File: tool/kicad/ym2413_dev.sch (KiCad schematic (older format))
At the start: 34 parts, among them P1 CONN_4, U1 YM2413, X1 CRYSTAL

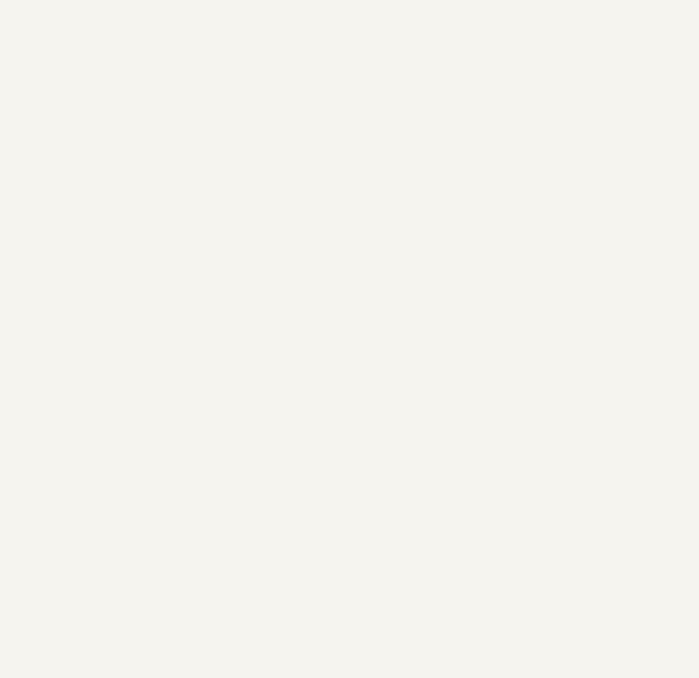
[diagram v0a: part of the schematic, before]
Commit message: add EFM32 to sch
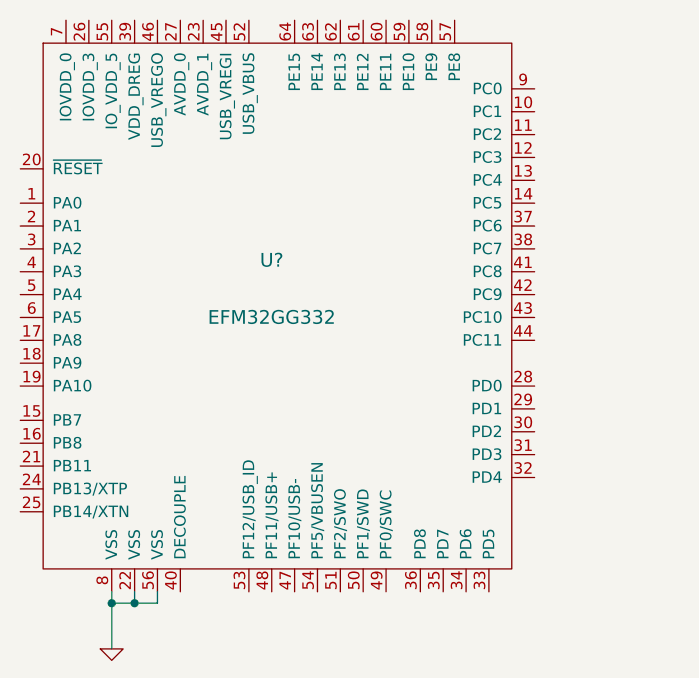
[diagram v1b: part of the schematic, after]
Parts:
- added U?: EFM32GG332, symbol EFM32GG332
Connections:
- wire segments 79 -> 83
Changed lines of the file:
@@
 	1    0    0    -1
 $EndComp
+$Comp
+L EFM32GG332 U?
+U 1 1 52F41304
+P 2500 4050
+F 0 "U?" H 2500 4150 60  0000 C CNN
+F 1 "EFM32GG332" H 2500 3900 60  0000 C CNN
+F 2 "" H 2100 4500 60  0000 C CNN
+F 3 "" H 2100 4500 60  0000 C CNN
+	1    2500 4050
+	1    0    0    -1
+$EndComp
+$Comp
+L GND #PWR?
+U 1 1 52F41311
+P 1800 5650
+F 0 "#PWR?" H 1800 5650 30  0001 C CNN
+F 1 "GND" H 1800 5580 30  0001 C CNN
+F 2 "" H 1800 5650 60  0000 C CNN
+F 3 "" H 1800 5650 60  0000 C CNN
+	1    1800 5650
+	1    0    0    -1
+$EndComp
+Wire Wire Line
+	1800 5650 1800 5400
+Wire Wire Line
+	1800 5450 2000 5450
+Wire Wire Line
+	2000 5450 2000 5400
+Connection ~ 1800 5450
+Wire Wire Line
+	1900 5400 1900 5450
+Connection ~ 1900 5450
 $EndSCHEMATC

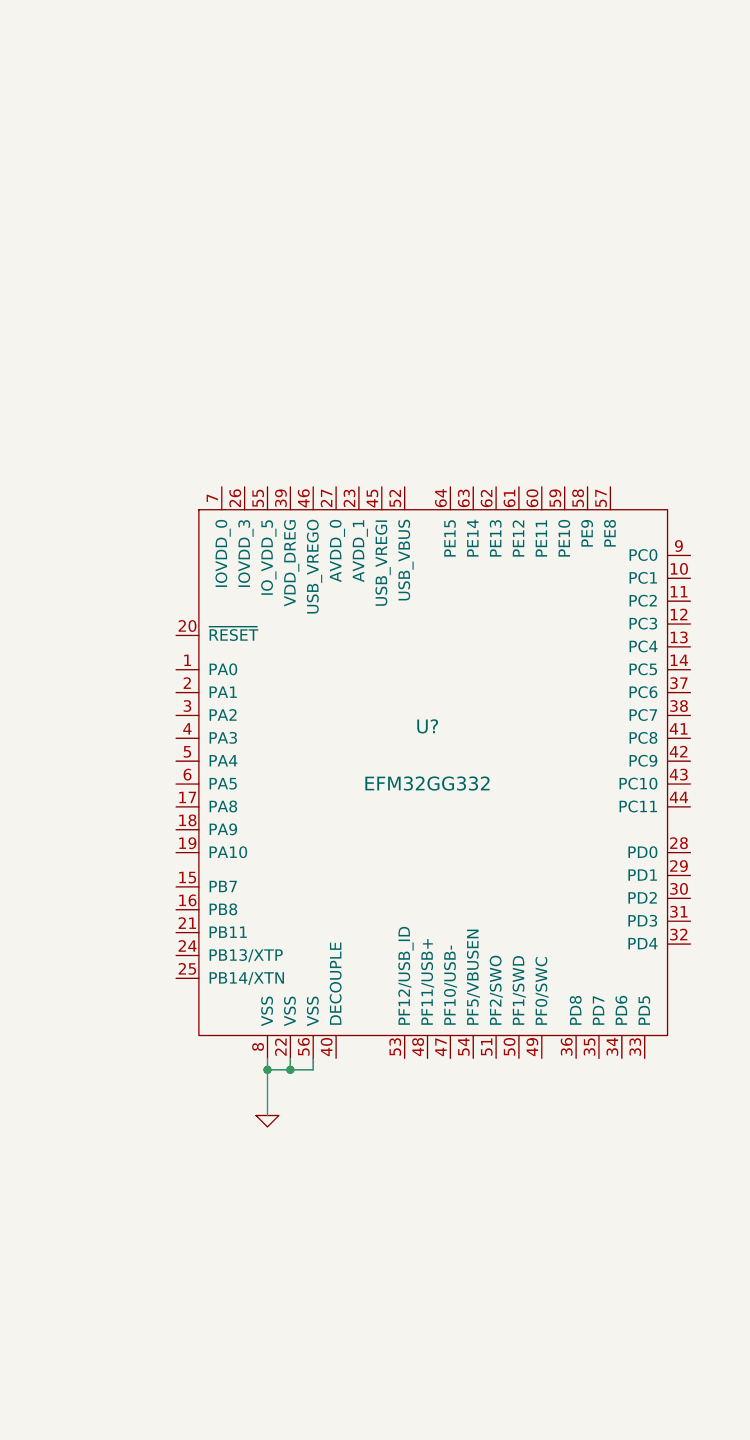
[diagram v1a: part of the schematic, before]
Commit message: add basic mcu perif
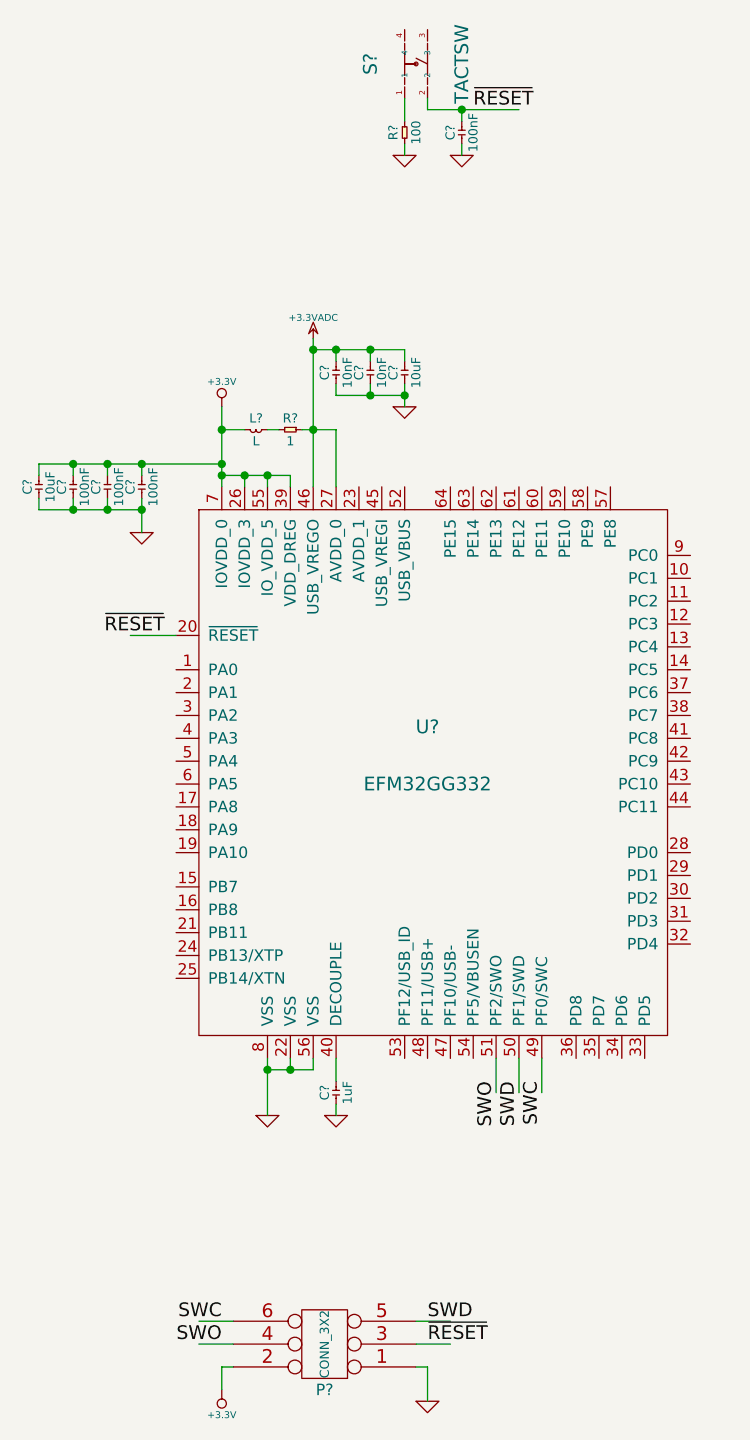
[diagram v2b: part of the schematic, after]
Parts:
- added C? (x4): 100nF, symbol C
- added C? (x2): 10uF, symbol C
- added C? (x2): 10nF, symbol C
- added C?: 1uF, symbol C
- added L?: L, symbol L
- added P?: CONN_3X2, symbol CONN_3X2
- added R?: 100, symbol R
- added R?: 1, symbol R
- added S?: TACTSW, symbol TACTSW
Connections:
- net labels added: +3.3V, +3.3VADC, SWC, SWD, SWO, ~RESET
- wire segments 83 -> 131

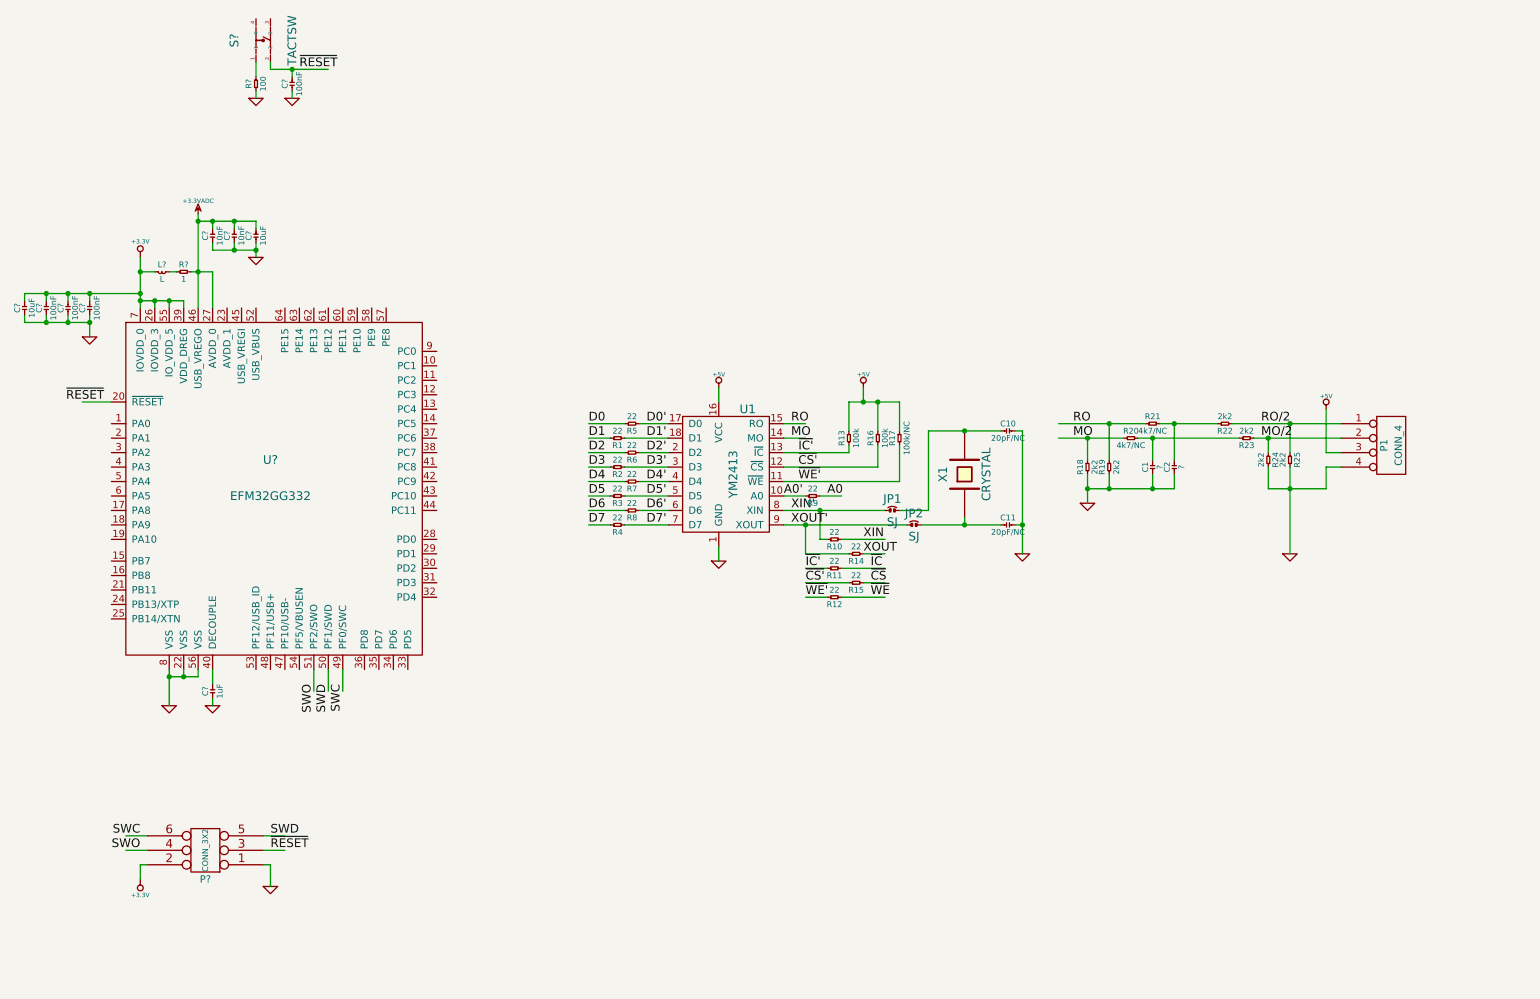
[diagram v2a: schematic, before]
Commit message: add 48Mhz xtal; add usb hardware design guidelines
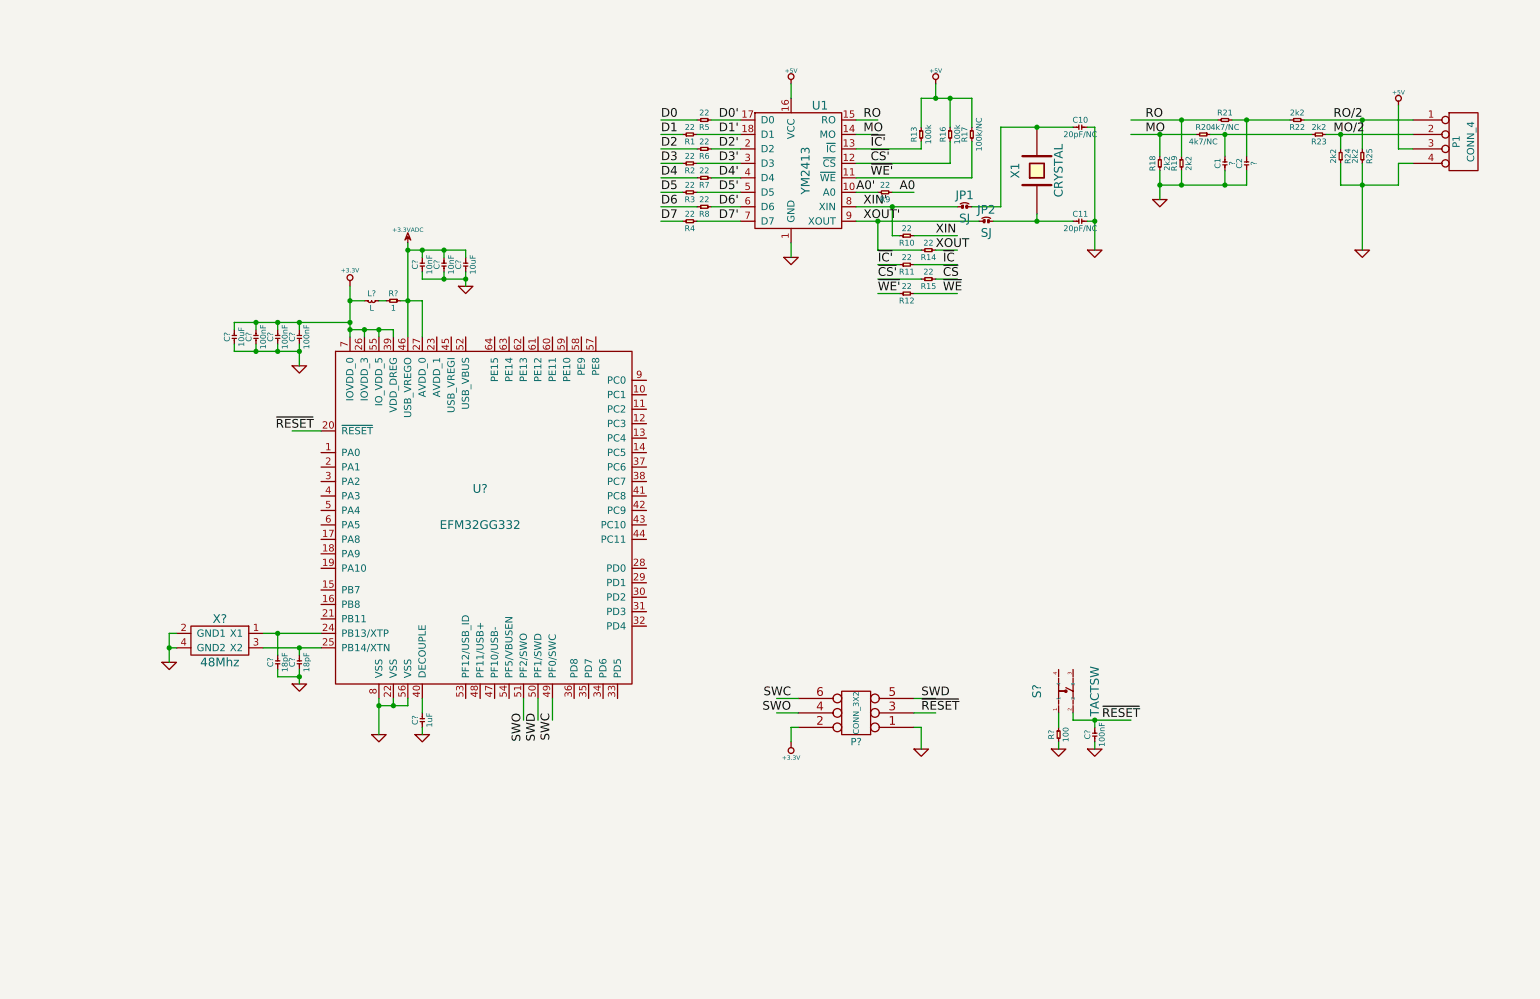
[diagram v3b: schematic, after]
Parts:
- added C? (x2): 18pF, symbol C
- added X?: 48Mhz, symbol TXC-XTAL
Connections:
- wire segments 131 -> 141
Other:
- moved on the sheet: C1, C10, C11, C2, C?, JP1, JP2, L?, P1, P?, R1, R10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

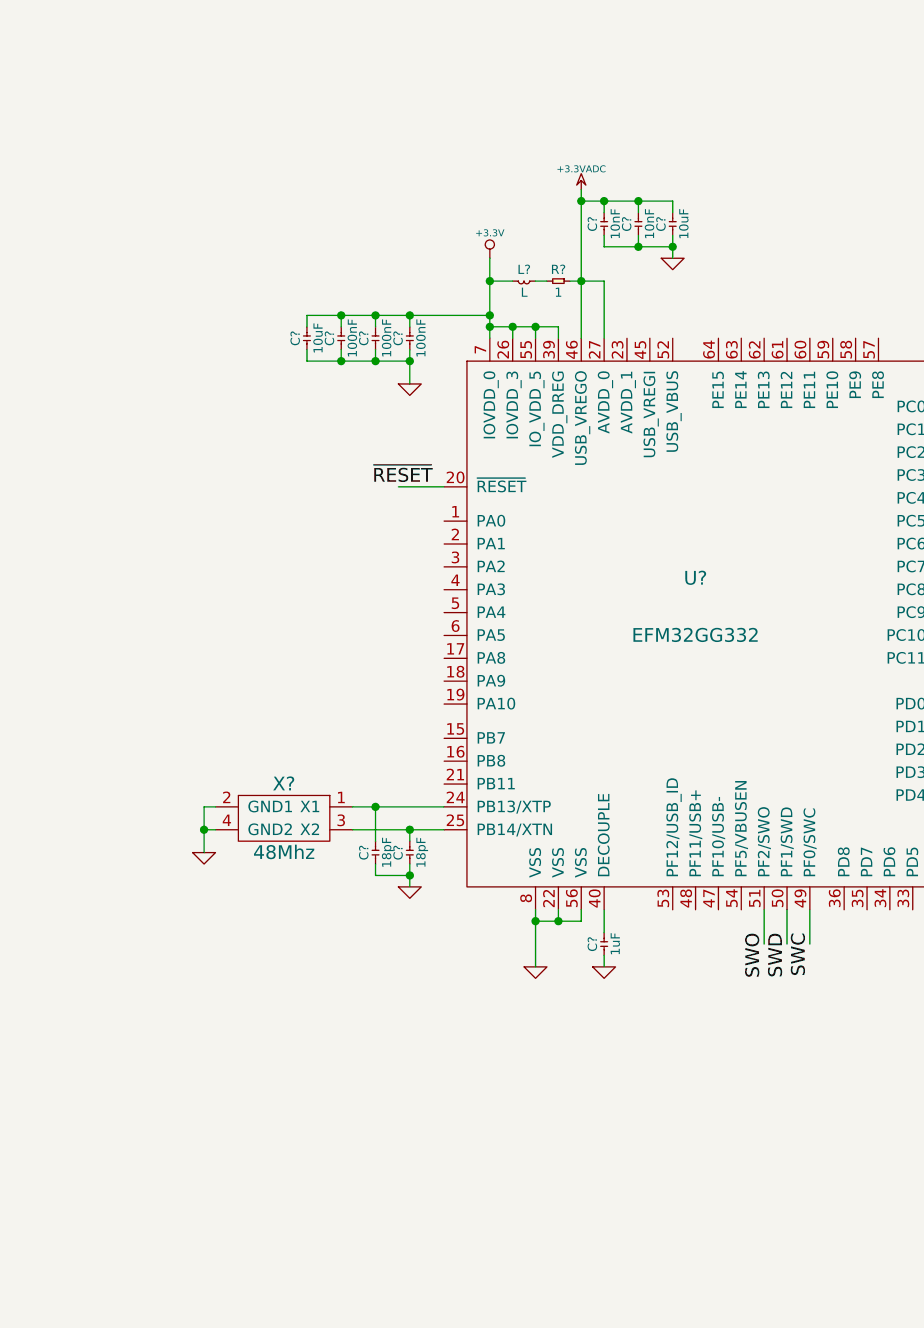
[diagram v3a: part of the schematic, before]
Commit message: create USB power circuitry and hook up USB power to efm32
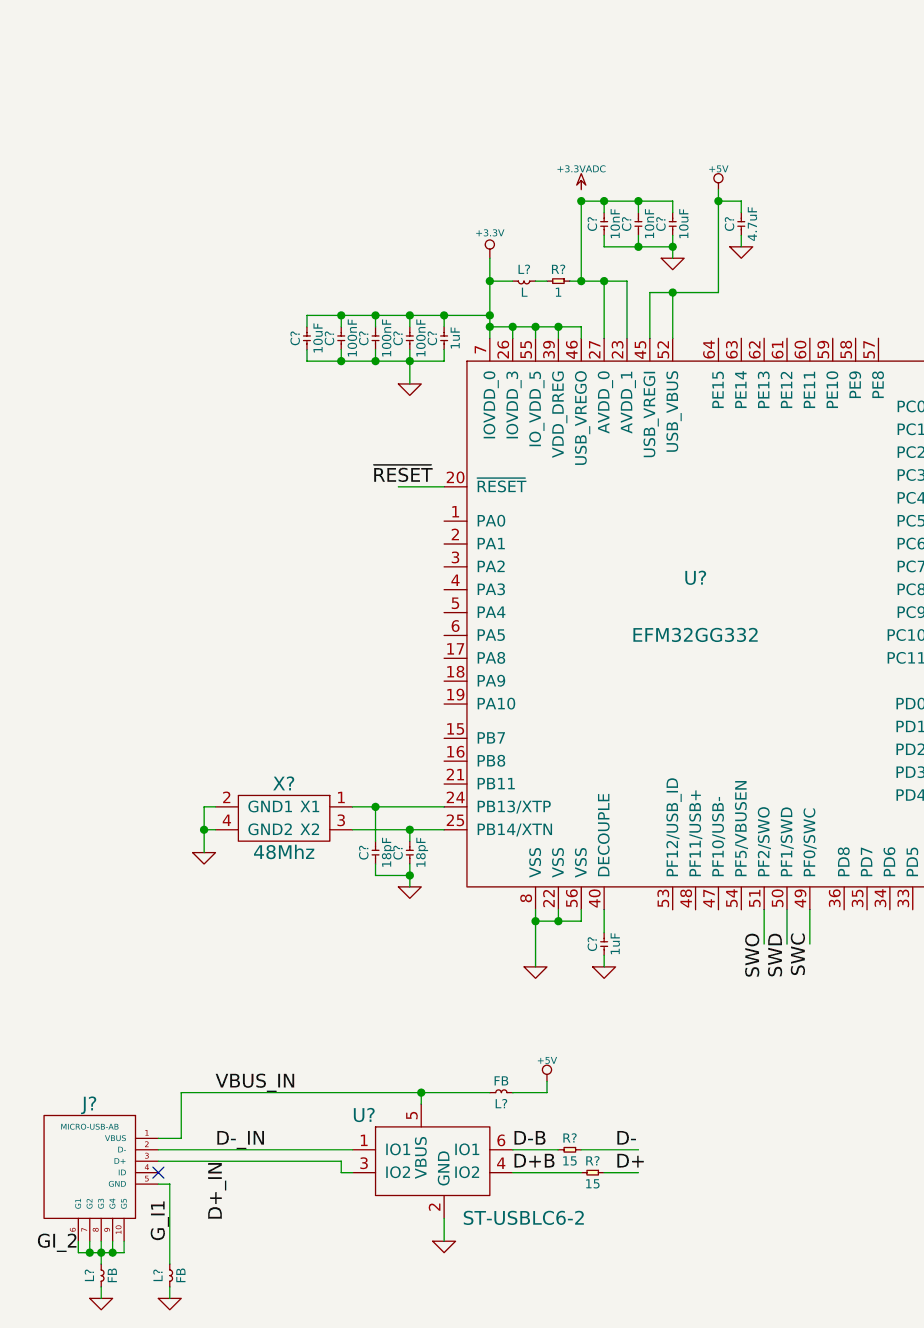
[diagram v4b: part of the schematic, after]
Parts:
- added C?: 4.7uF, symbol C
- added C?: 1uF, symbol C
- added J?: MICRO-USB-AB, symbol MICRO-USB-AB
- added L? (x3): FB, symbol L
- added R? (x2): 15, symbol R
- added U?: ST-USBLC6-2, symbol ST-USBLC6-2
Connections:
- net labels added: D+, D+B, D+_IN, D-, D-B, D-_IN, GI_2, G_I1, VBUS_IN
- wire segments 141 -> 177
- no-connect marks 0 -> 1

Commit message: hook up usb- and usb+
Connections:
- wire segments 177 -> 179
- no-connect marks 1 -> 3
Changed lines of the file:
@@
 $EndComp
 Wire Wire Line
-	3450 6650 3700 6650
+	3450 6650 4050 6650
 Wire Wire Line
-	3700 6750 3550 6750
+	3550 6750 3950 6750
 Text Label 3150 6650 0    60   ~ 0
 D-B
@@
 	3850 2900 3850 3100
 Connection ~ 3850 2900
+NoConn ~ 4150 5600
+NoConn ~ 3850 5600
+Wire Wire Line
+	4050 6650 4050 5600
+Wire Wire Line
+	3950 6750 3950 5600
 $EndSCHEMATC
